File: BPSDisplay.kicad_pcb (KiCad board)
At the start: 2 copper layers, 85 x 56 mm, 55 parts, among them J1 SWD, J2 Conn_02x06_Counter_Clockwise, J3 CAN_Out, J5 CarPowerConnector, P1 Conn_02x20_Odd_Even, SW1 Reset, U1 STM32F413RHTx, U2 ADM3055E, U3 CDSOT23-T24CAN, U6 PDS1-S12-S5, U7 NCP1117-3.3_SOT223, Y1 8M

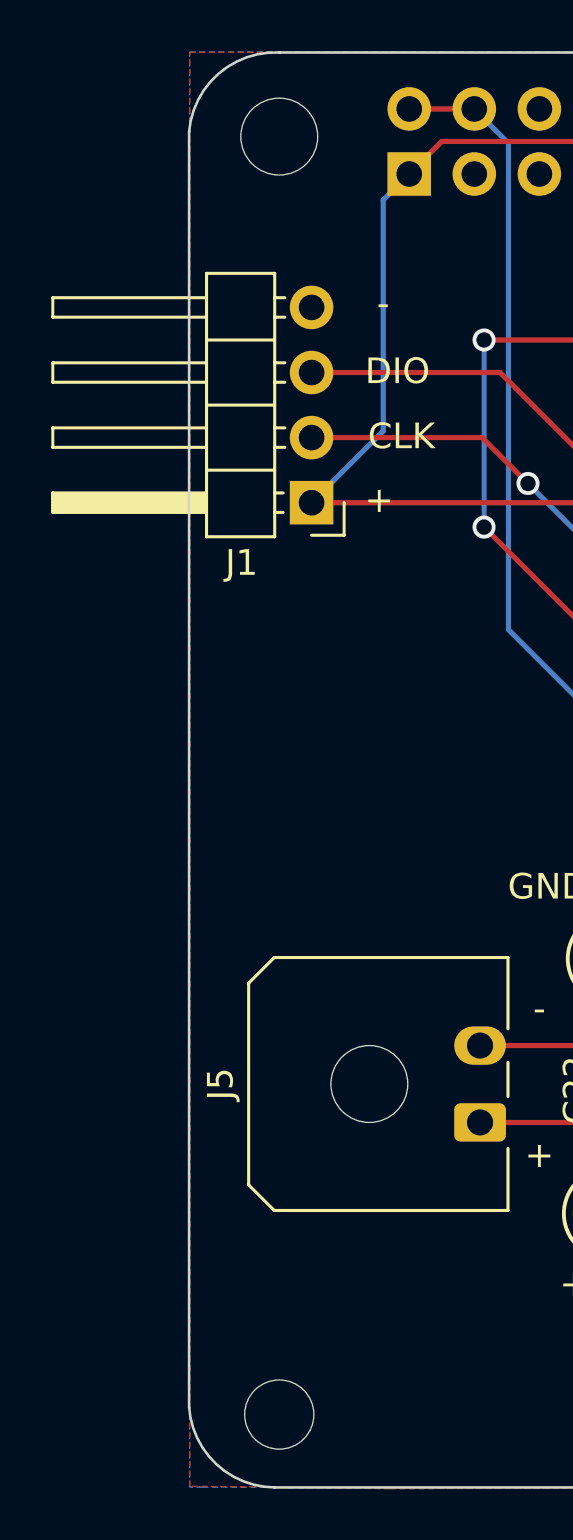
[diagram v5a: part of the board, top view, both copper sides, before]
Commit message: Making left edge cut straight
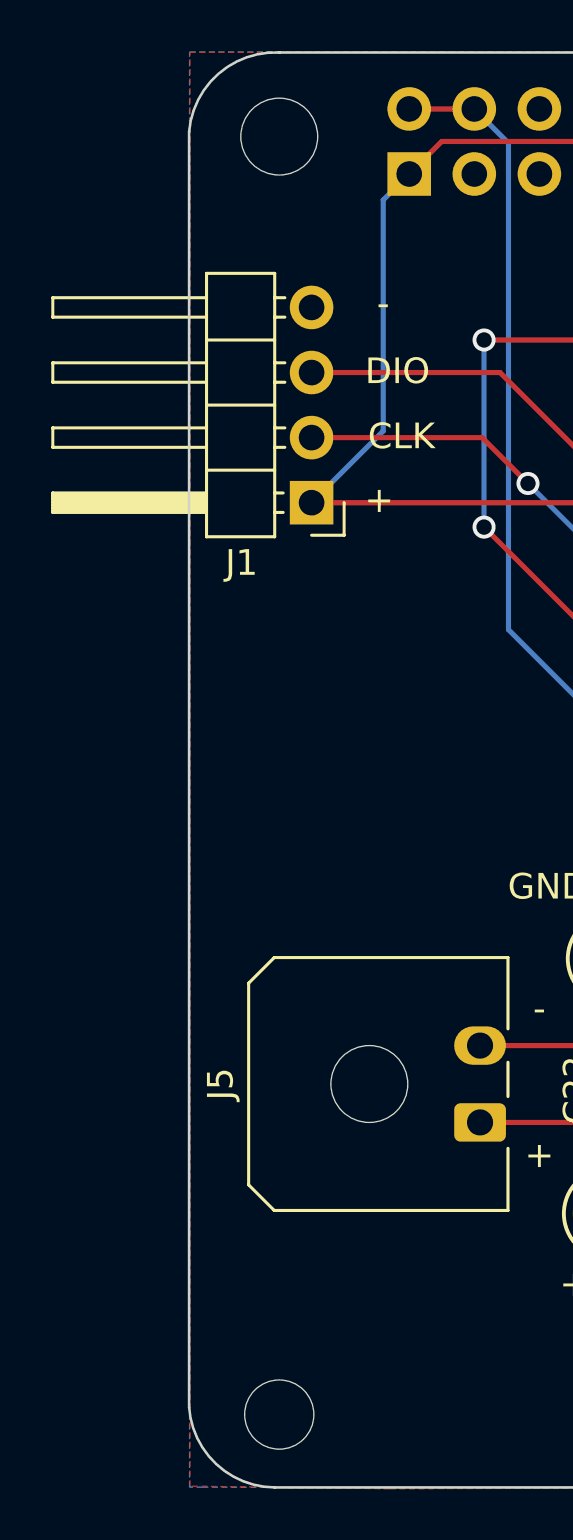
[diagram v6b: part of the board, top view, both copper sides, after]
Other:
- net class Default: clearance 0.2 -> 0.127
- rule trace_clearance: 0.2 -> 0.127

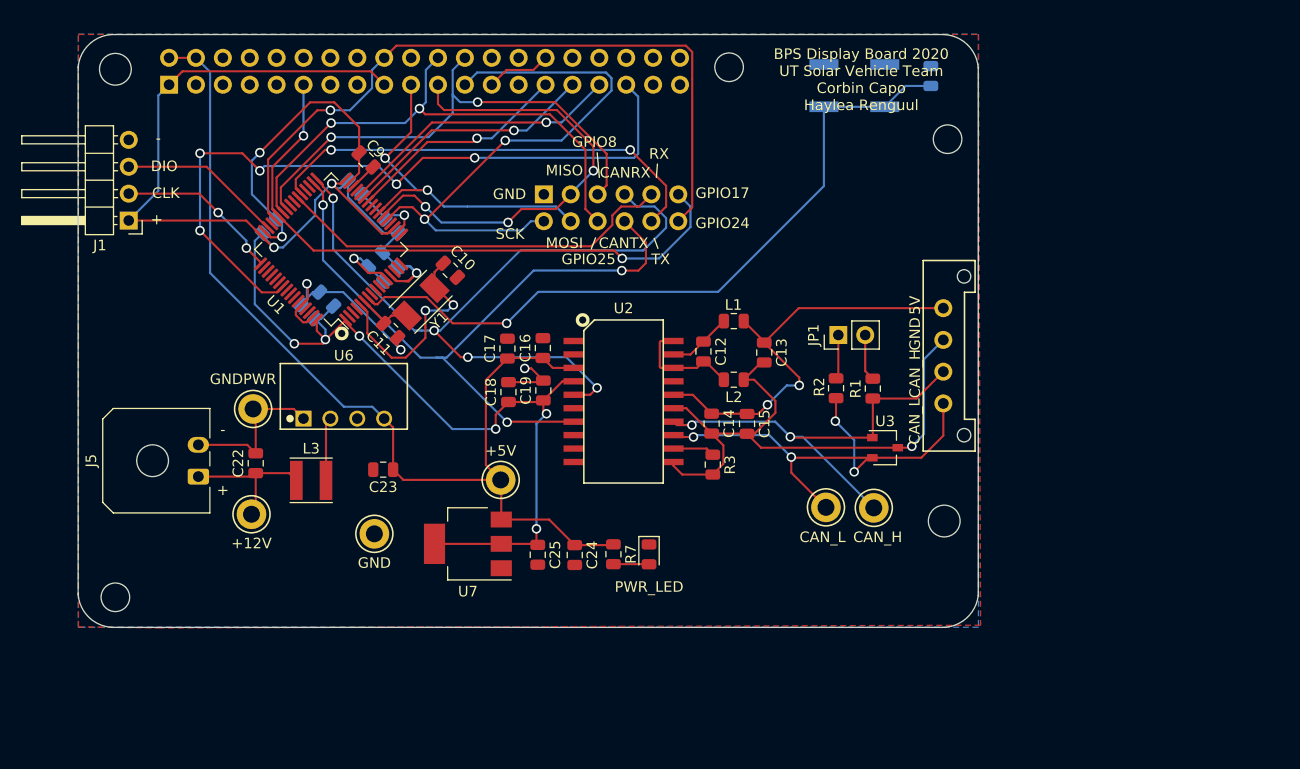
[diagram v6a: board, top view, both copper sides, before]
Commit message: Editing PCB layout
Moved mounting holes into the correct order/spots, moved U6 closer to the left edge of the board (since it's a taller component), removed the sharp angle near C17
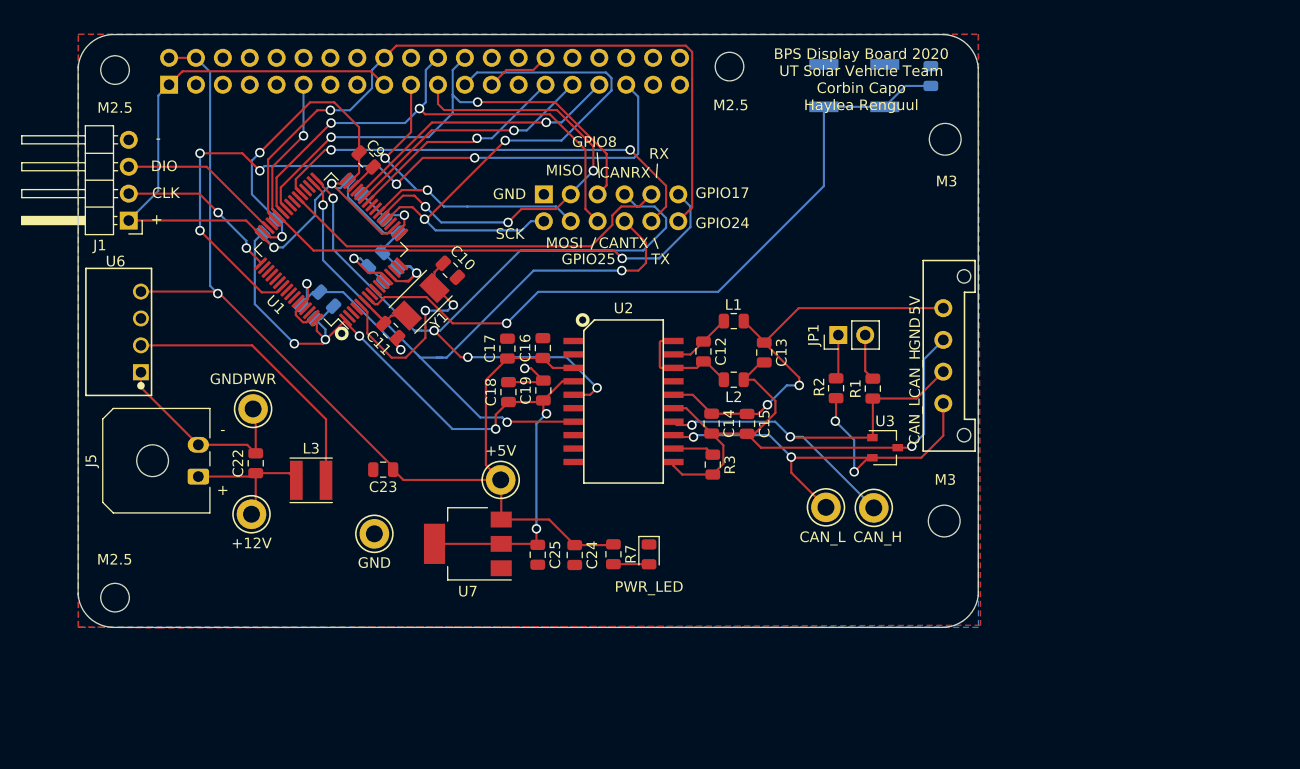
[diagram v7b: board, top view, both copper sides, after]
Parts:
- moved MK1 78.9 mm to (199.5, 108.4)
- moved MK3 78.7 mm to (277.9, 114.9)
- moved MK4 76.7 mm to (257.5, 108.0)
- moved MK2 76.6 mm to (199.5, 158.2)
- moved U6 20.8 mm to (201.9, 133.1), turned to 90 degrees
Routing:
- net Net-(L3-Pad2): track 6.00 -> 28.4 mm
- net +5V: track 96.2 -> 102.1 mm, vias 0 -> 1
- net GNDPWR: track 15.2 -> 19.1 mm
- net /CAN2_TX: track 66.8 -> 69.3 mm
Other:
- board text added: "M2.5"
- board text added: "M3"

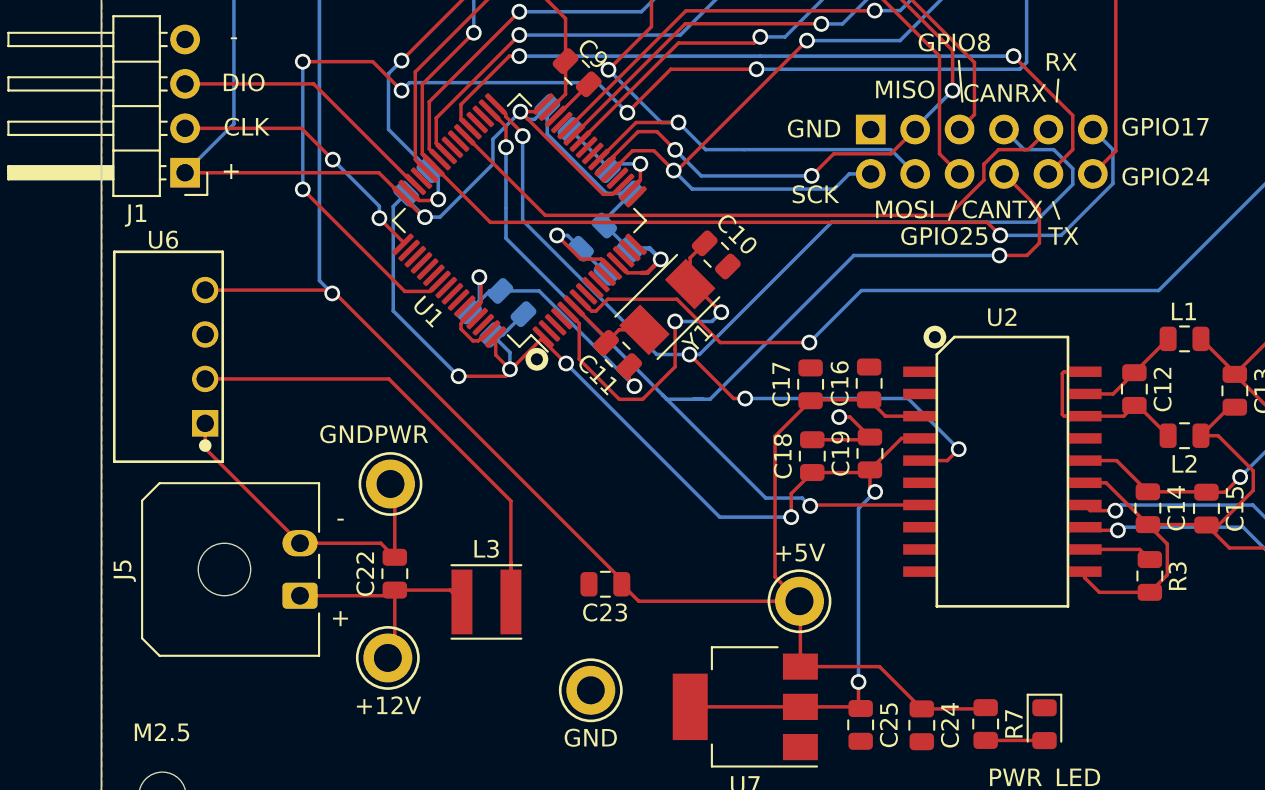
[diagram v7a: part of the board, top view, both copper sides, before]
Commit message: Removed traces under Y1
Also aligned J5 with U6
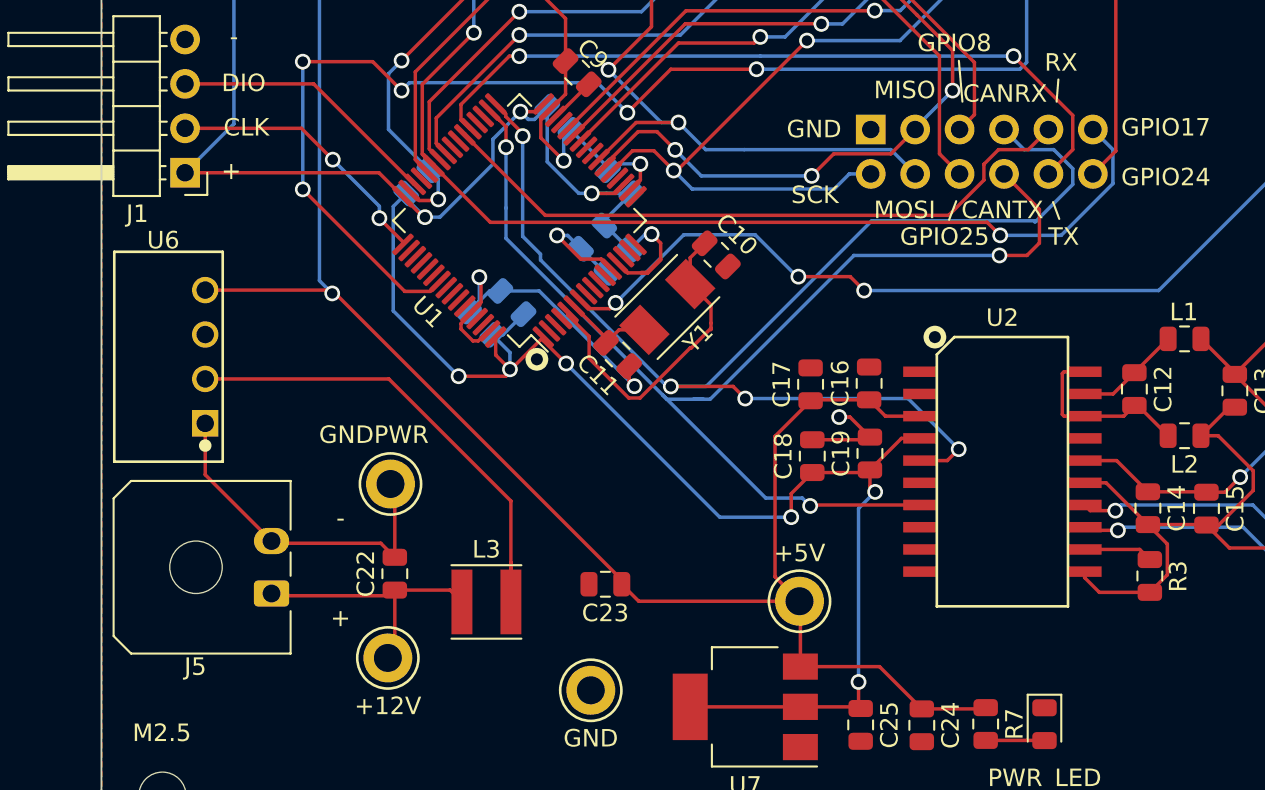
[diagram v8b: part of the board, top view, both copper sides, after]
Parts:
- moved J5 1.63 mm to (205.7, 146.6)
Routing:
- net GND: track 76.9 -> 82.5 mm, vias 7 -> 8
- net +3V3: track 167.7 -> 164.2 mm, vias 9 -> 10
- net /CAN2_RX: track 71.8 -> 74.8 mm
- net +12V: track 13.7 -> 15.4 mm
- net Net-(C10-Pad1): track 20.7 -> 19.4 mm, vias 2 -> 0
- net GNDPWR: track 19.1 -> 20.0 mm
- net /NRST: track 68.4 -> 69.0 mm, vias 1 -> 3
